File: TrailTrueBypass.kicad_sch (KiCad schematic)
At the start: 52 parts, among them J1 Conn_01x05_Pin, J2 Conn_01x05_Pin, J3 Conn_02x03_Top_Bottom, K1 G6S-2, K2 G6S-2, K3 G6S-2, Q1 2N3904, Q2 2N3904, Q3 2N3904, U1 Opamp_Quad, U2 MC78L05_SOT89, U3 PIC12F675-xP

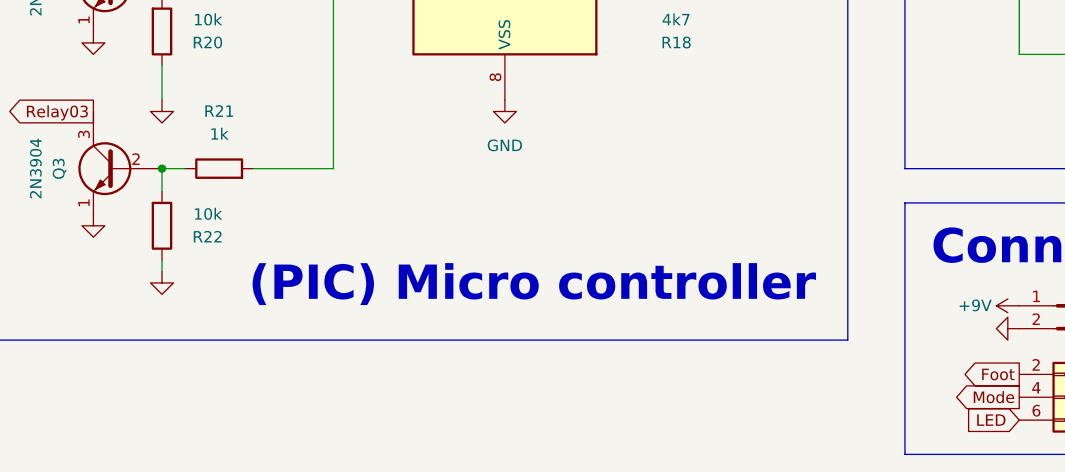
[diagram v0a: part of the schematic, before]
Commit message: update: schファイルの軽微な修正
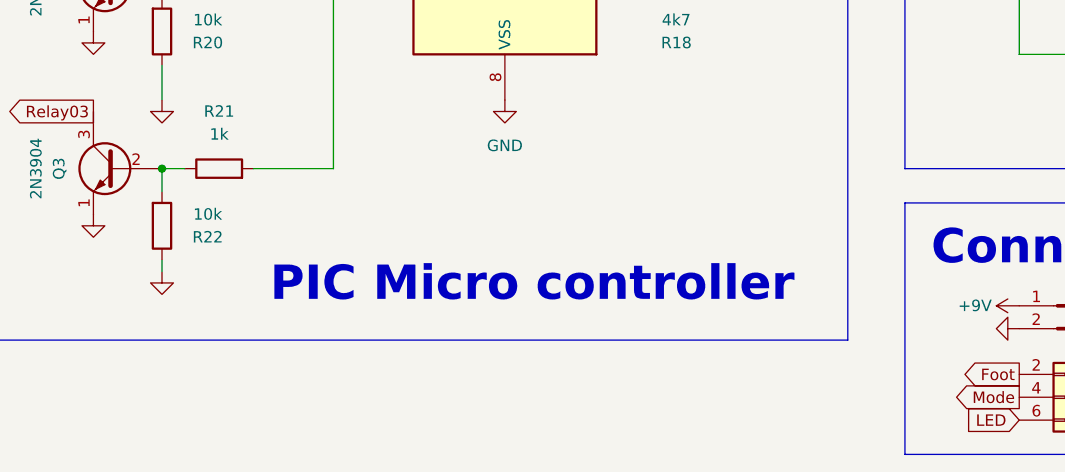
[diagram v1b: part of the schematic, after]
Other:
- note added: "PIC Micro controller"
- note removed: "(PIC) Micro controller"
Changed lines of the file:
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@@
 		)
 	)
-	(text "(PIC) Micro controller"
+	(text "PIC Micro controller"
 		(exclude_from_sim no)
 		(at 91.948 171.704 0)
